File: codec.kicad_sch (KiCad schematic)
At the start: 10 parts, among them U301 PCM3060

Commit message: Review PSU, add footprints for all components
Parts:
- U301: PN (none) -> PCM3060PW
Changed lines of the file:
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@@
+      (effects (font (size 1.27 1.27)) hide)
+    )
+    (property "PN" "PCM3060PW" (id 4) (at 133.35 123.19 0)
       (effects (font (size 1.27 1.27)) hide)
     )

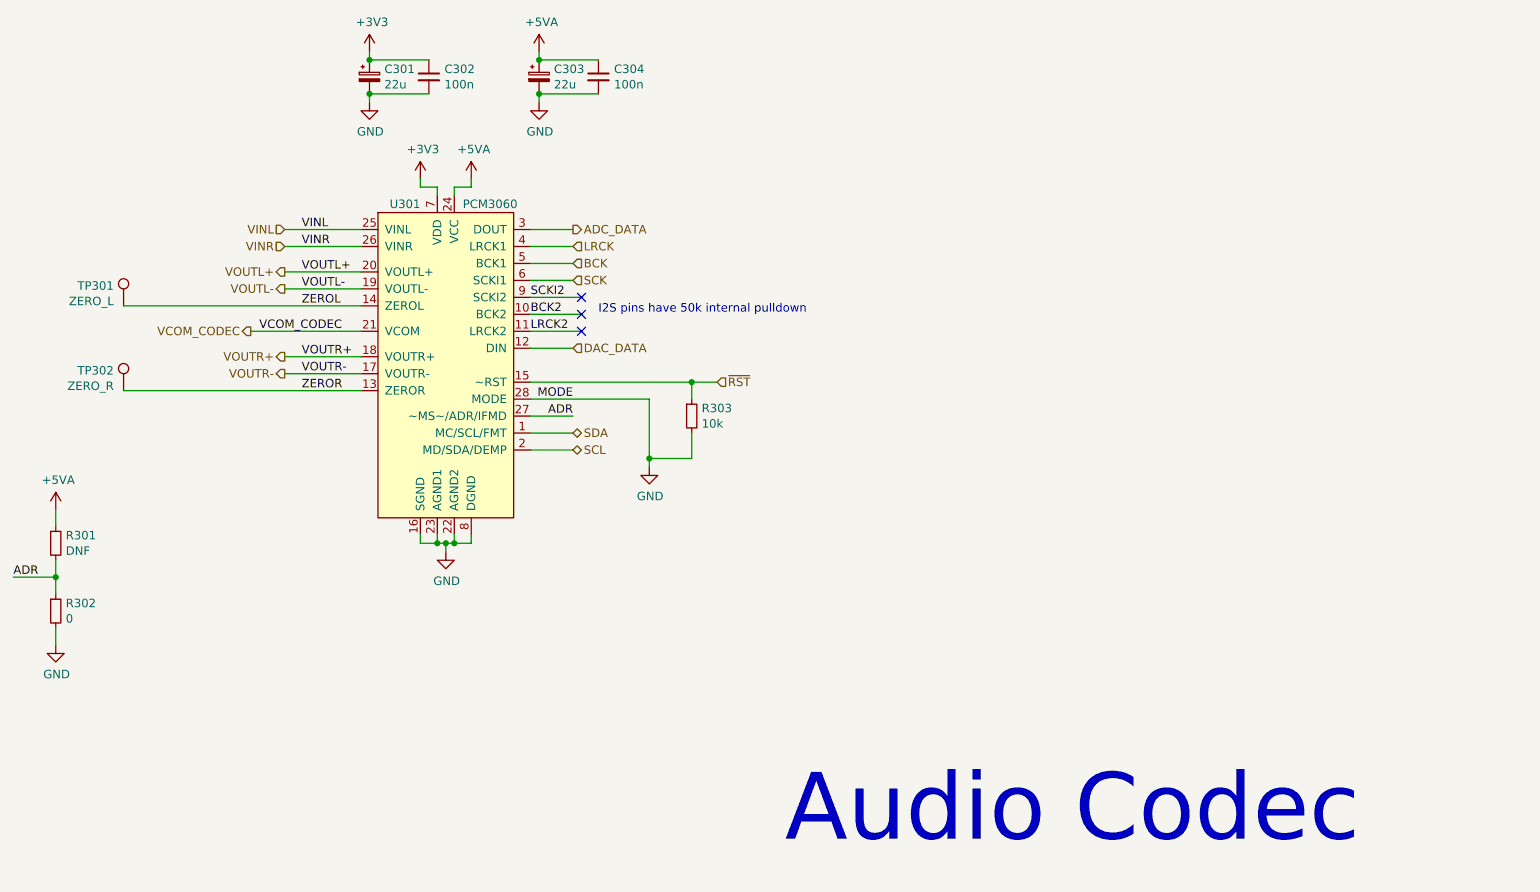
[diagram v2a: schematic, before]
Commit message: Schematic reviewed, assign PN to all parts
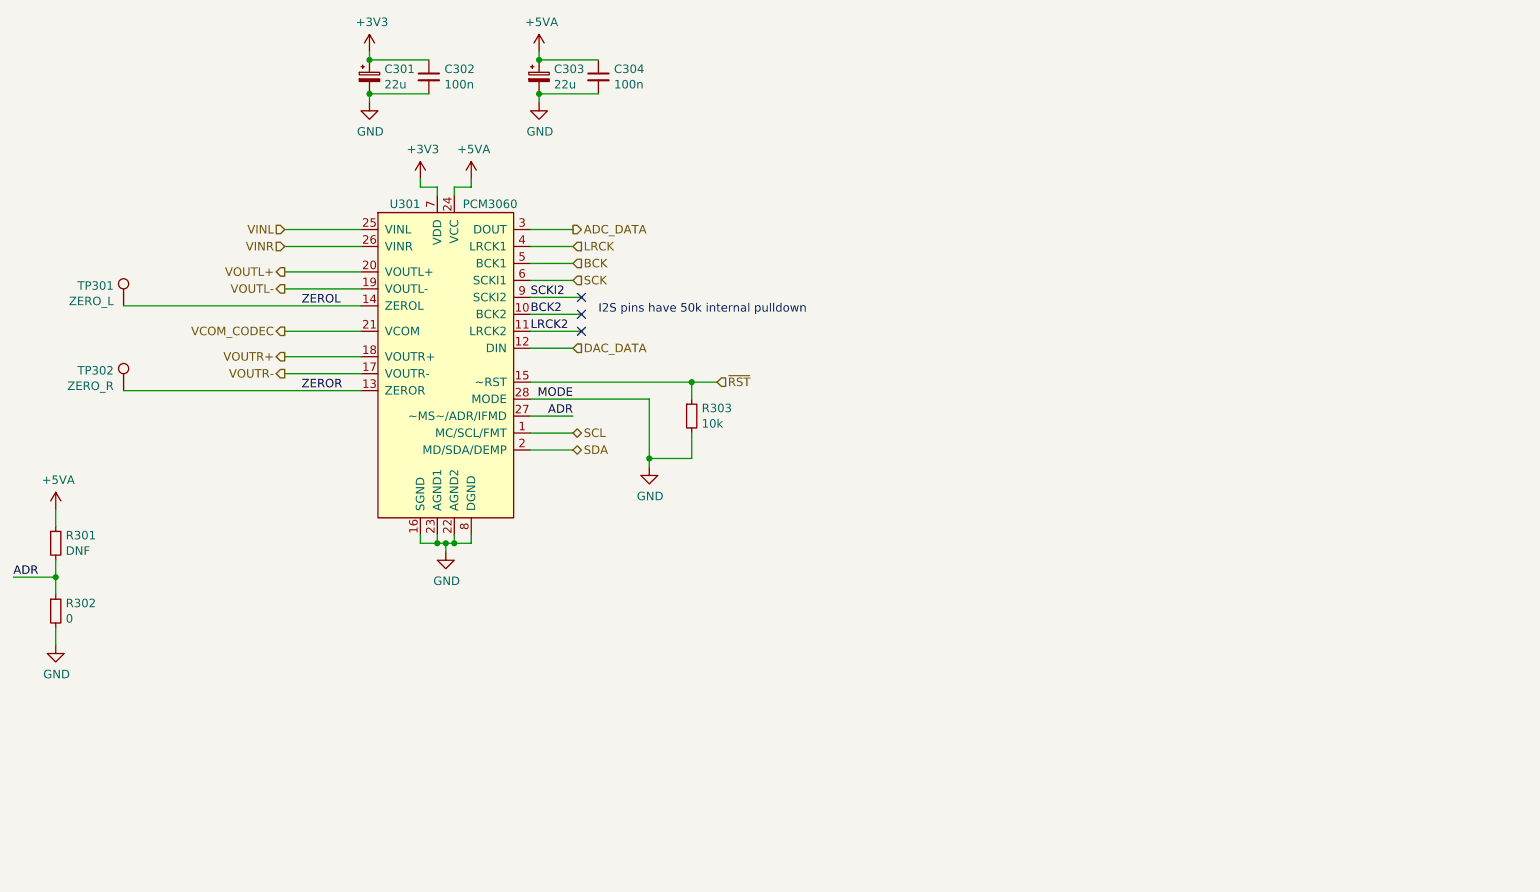
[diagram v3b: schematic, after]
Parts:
- R301: now left out of the parts list
- R302: PN (none) -> CR0805-J/-000ELF
- R303: PN (none) -> CR0805-FX-1002ELF
- TP301, TP302: footprint guitar_dsp_platform:TestPoint_THTPad_D2.0mm_Drill1.0mm -> TestPoint:TestPoint_Pad_1.0x1.0mm; now left out of the parts list
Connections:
- net SCL: now also U301.1 (MC/SCL/FMT); no longer U301.2 (MD/SDA/DEMP)
- net SDA: now also U301.2 (MD/SDA/DEMP); no longer U301.1 (MC/SCL/FMT)
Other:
- note removed: "Audio Codec"
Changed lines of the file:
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@@
-    (stroke (width 0) (type solid) (color 0 0 0 0))
-  )
-  (wire (pts (xy 104.14 105.41) (xy 120.65 105.41))
     (stroke (width 0) (type solid) (color 0 0 0 0))
   )
@@
     (stroke (width 0) (type solid) (color 0 0 0 0))
   )
+  (wire (pts (xy 109.22 105.41) (xy 120.65 105.41))
+    (stroke (width 0) (type solid) (color 0 0 0 0))
+  )
   (wire (pts (xy 109.22 109.22) (xy 120.65 109.22))
     (stroke (width 0) (type solid) (color 0 0 0 0))
@@
     (stroke (width 0) (type solid) (color 0 0 0 0))
   )
-  (wire (pts (xy 146.05 120.65) (xy 152.4 120.65))
+  (wire (pts (xy 146.05 123.19) (xy 152.4 123.19))
     (stroke (width 0) (type solid) (color 0 0 0 0))
   )
@@
     (stroke (width 0) (type solid) (color 0 0 0 0))
   )
-  (wire (pts (xy 152.4 123.19) (xy 146.05 123.19))
+  (wire (pts (xy 152.4 120.65) (xy 146.05 120.65))
     (stroke (width 0) (type solid) (color 0 0 0 0))
   )
@@
     (effects (font (size 1.27 1.27)) (justify left bottom))
   )
-  (text "Audio Codec" (at 184.15 182.88 0)
-    (effects (font (size 10.0076 10.0076)) (justify left bottom))
-  )
   (label "ADR" (at 68.58 142.24 0)
     (effects (font (size 1.27 1.27)) (justify left bottom))
   )
-  (label "VCOM_CODEC" (at 105.41 105.41 0)
-    (effects (font (size 1.27 1.27)) (justify left bottom))
-  )
-  (label "VINL" (at 111.76 90.17 0)
-    (effects (font (size 1.27 1.27)) (justify left bottom))
-  )
-  (label "VINR" (at 111.76 92.71 0)
-    (effects (font (size 1.27 1.27)) (justify left bottom))
-  )
-  (label "VOUTL+" (at 111.76 96.52 0)
-    (effects (font (size 1.27 1.27)) (justify left bottom))
-  )
-  (label "VOUTL-" (at 111.76 99.06 0)
-    (effects (font (size 1.27 1.27)) (justify left bottom))
-  )
   (label "ZEROL" (at 111.76 101.6 0)
-    (effects (font (size 1.27 1.27)) (justify left bottom))
-  )
-  (label "VOUTR+" (at 111.76 109.22 0)
-    (effects (font (size 1.27 1.27)) (justify left bottom))
-  )
-  (label "VOUTR-" (at 111.76 111.76 0)
     (effects (font (size 1.27 1.27)) (justify left bottom))
   )
@@
     (effects (font (size 1.27 1.27)) (justify right bottom))
   )
-  (hierarchical_label "VCOM_CODEC" (shape output) (at 104.14 105.41 180)
-    (effects (font (size 1.27 1.27)) (justify right))
-  )
   (hierarchical_label "VINL" (shape input) (at 109.22 90.17 180)
     (effects (font (size 1.27 1.27)) (justify right))
@@
     (effects (font (size 1.27 1.27)) (justify right))
   )
+  (hierarchical_label "VCOM_CODEC" (shape output) (at 109.22 105.41 180)
+    (effects (font (size 1.27 1.27)) (justify right))
+  )
   (hierarchical_label "VOUTR+" (shape output) (at 109.22 109.22 180)
     (effects (font (size 1.27 1.27)) (justify right))
@@
     (effects (font (size 1.27 1.27)) (justify left))
   )
-  (hierarchical_label "SDA" (shape tri_state) (at 152.4 120.65 0)
-    (effects (font (size 1.27 1.27)) (justify left))
-  )
-  (hierarchical_label "SCL" (shape tri_state) (at 152.4 123.19 0)
+  (hierarchical_label "SCL" (shape tri_state) (at 152.4 120.65 0)
+    (effects (font (size 1.27 1.27)) (justify left))
+  )
+  (hierarchical_label "SDA" (shape tri_state) (at 152.4 123.19 0)
     (effects (font (size 1.27 1.27)) (justify left))
   )
@@
   )
   (symbol (lib_id "Connector:TestPoint") (at 85.09 101.6 0) (mirror y) (unit 1)
-    (in_bom yes) (on_board yes)
+    (in_bom no) (on_board yes)
     (property "Reference" "TP301" (id 0) (at 83.6168 98.6028 0)
       (effects (font (size 1.27 1.27)) (justify left))
@@
       (effects (font (size 1.27 1.27)) (justify left))
     )
-    (property "Footprint" "guitar_dsp_platform:TestPoint_THTPad_D2.0mm_Drill1.0mm" (id 2) (at 80.01 101.6 0)
+    (property "Footprint" "TestPoint:TestPoint_Pad_1.0x1.0mm" (id 2) (at 80.01 101.6 0)
       (effects (font (size 1.27 1.27)) hide)
     )
@@
   )
   (symbol (lib_id "Connector:TestPoint") (at 85.09 114.3 0) (mirror y) (unit 1)
-    (in_bom yes) (on_board yes)
+    (in_bom no) (on_board yes)
     (property "Reference" "TP302" (id 0) (at 83.6168 111.3028 0)
       (effects (font (size 1.27 1.27)) (justify left))
@@
       (effects (font (size 1.27 1.27)) (justify left))
     )
-    (property "Footprint" "guitar_dsp_platform:TestPoint_THTPad_D2.0mm_Drill1.0mm" (id 2) (at 80.01 114.3 0)
-      (effects (font (size 1.27 1.27)) hide)
-    )
-    (property "Datasheet" "~" (id 3) (at 80.01 114.3 0)
+    (property "Footprint" "TestPoint:TestPoint_Pad_1.0x1.0mm" (id 2) (at 80.01 114.3 0)
+      (effects (font (size 1.27 1.27)) hide)
+    )
+    (property "Datasheet" "" (id 3) (at 80.01 114.3 0)
       (effects (font (size 1.27 1.27)) hide)
     )
@@
   )
   (symbol (lib_id "Device:R_Small") (at 74.93 137.16 0) (unit 1)
-    (in_bom yes) (on_board yes)
+    (in_bom no) (on_board yes)
     (property "Reference" "R301" (id 0) (at 76.4286 135.9916 0)
       (effects (font (size 1.27 1.27)) (justify left))
@@
       (effects (font (size 1.27 1.27)) hide)
     )
+    (property "PN" "CR0805-J/-000ELF" (id 4) (at 74.93 147.32 0)
+      (effects (font (size 1.27 1.27)) hide)
+    )
     (pin "1")
     (pin "2")
@@
       (effects (font (size 1.27 1.27)) hide)
     )
+    (property "PN" "CR0805-FX-1002ELF" (id 4) (at 170.18 118.11 0)
+      (effects (font (size 1.27 1.27)) hide)
+    )

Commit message: Update some part numbers for in-stock parts
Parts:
- C301, C303: PN EEEFK1A220R -> EEEFK1A220AR
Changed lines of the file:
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@@
       (effects (font (size 1.27 1.27)) hide)
     )
-    (property "Datasheet" "https://industrial.panasonic.com/cdbs/www-data/pdf/RDE0000/ABA0000C1181.pdf" (id 3) (at 121.92 67.31 0)
+    (property "Datasheet" "https://www.mouser.co.uk/datasheet/2/315/ABA0000C1175-947561.pdf" (id 3) (at 121.92 67.31 0)
       (effects (font (size 1.27 1.27)) hide)
     )
-    (property "PN" "EEEFK1A220R" (id 4) (at 121.92 67.31 0)
+    (property "PN" "EEEFK1A220AR" (id 4) (at 121.92 67.31 0)
       (effects (font (size 1.27 1.27)) hide)
     )
@@
       (effects (font (size 1.27 1.27)) hide)
     )
-    (property "Datasheet" "https://industrial.panasonic.com/cdbs/www-data/pdf/RDE0000/ABA0000C1181.pdf" (id 3) (at 147.32 67.31 0)
+    (property "Datasheet" "https://www.mouser.co.uk/datasheet/2/315/ABA0000C1175-947561.pdf" (id 3) (at 147.32 67.31 0)
       (effects (font (size 1.27 1.27)) hide)
     )
-    (property "PN" "EEEFK1A220R" (id 4) (at 147.32 67.31 0)
+    (property "PN" "EEEFK1A220AR" (id 4) (at 147.32 67.31 0)
       (effects (font (size 1.27 1.27)) hide)
     )
